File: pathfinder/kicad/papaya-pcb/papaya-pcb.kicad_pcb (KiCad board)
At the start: 2 copper layers, 70 x 90 mm, 12 parts, among them J1 J1, J10 J_S2, J11 J_S3, J12 J_S4, J2 J_ESP32, J3 J_UBEC5V, J4 J_BTS1, J5 J_BTS2, J6 J_ELRS, J7 J_GND_MASTER, J8 J_UBEC6V, J9 J_S1

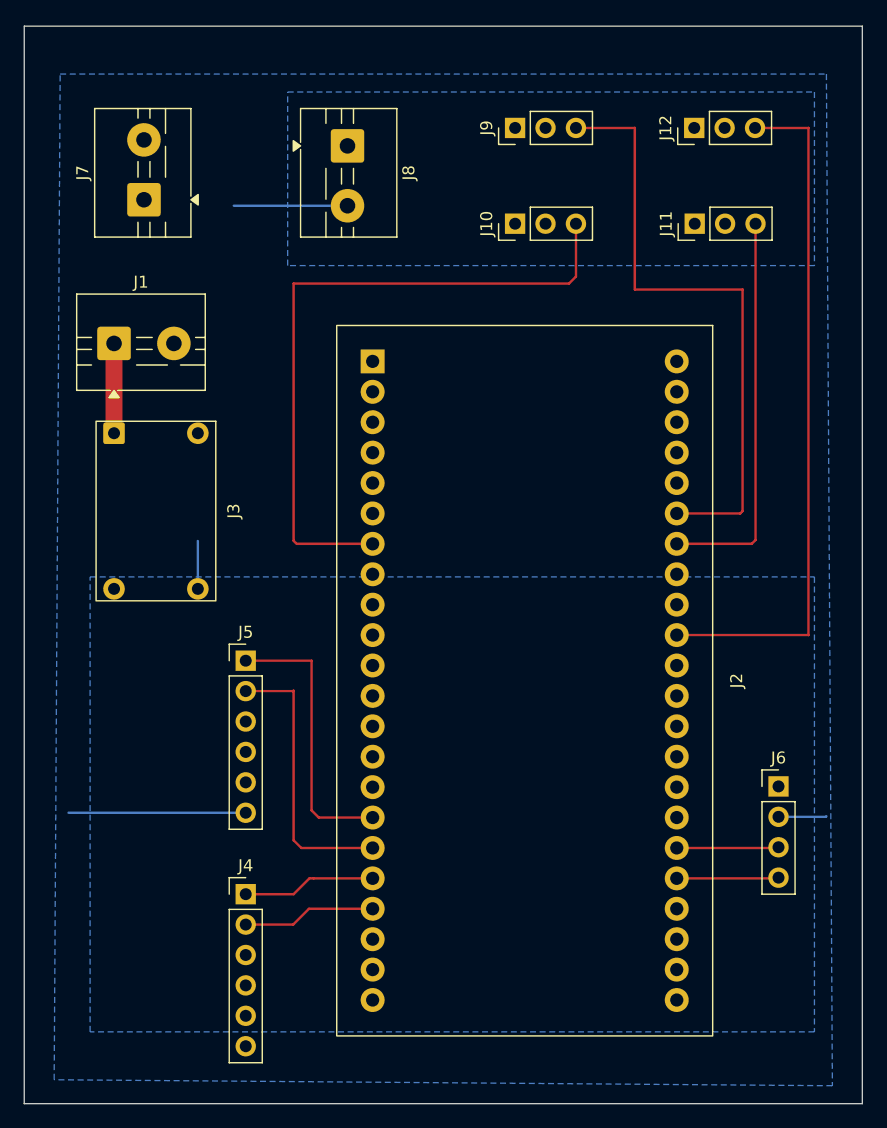
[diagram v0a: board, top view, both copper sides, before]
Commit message: Add M3 mounting holes at PCB corners
Four 3.2mm (M3 clearance) NPTH mounting holes (H1-H4) placed at the
board corners for chassis mounting. J7 and the servo header cluster
(J9-J12) were nudged to clear the new holes; zones refilled and
re-verified via DRC (0 violations).
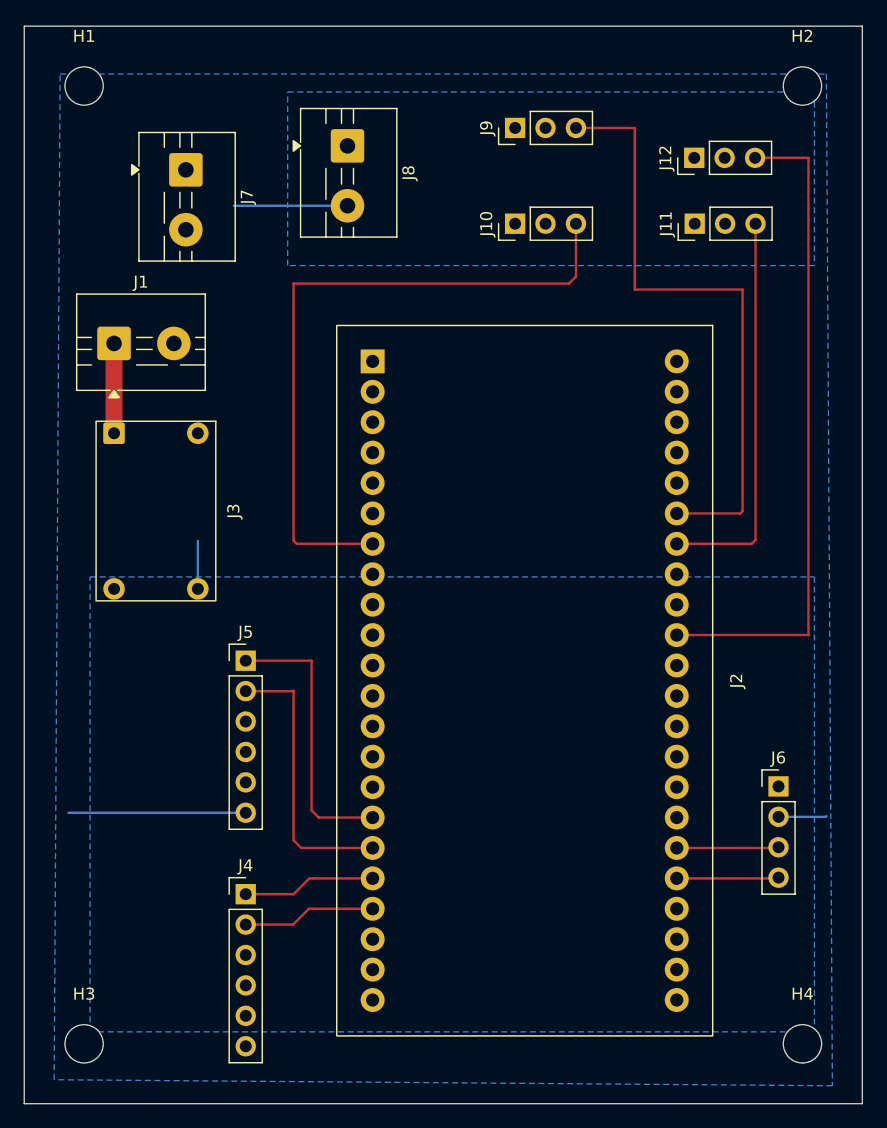
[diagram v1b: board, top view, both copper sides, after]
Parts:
- added H1: MountingHole_3.2mm_M3, MountingHole:MountingHole_3.2mm_M3, F.Cu at (95.5, 63.5)
- added H2: MountingHole_3.2mm_M3, MountingHole:MountingHole_3.2mm_M3, F.Cu at (155.5, 63.5)
- added H3: MountingHole_3.2mm_M3, MountingHole:MountingHole_3.2mm_M3, F.Cu at (95.5, 143.5)
- added H4: MountingHole_3.2mm_M3, MountingHole:MountingHole_3.2mm_M3, F.Cu at (155.5, 143.5)
- moved J7 4.30 mm to (104.0, 70.5), turned to -90 degrees
- moved J12 2.50 mm to (146.5, 69.5)
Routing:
- net /NET_S4_SIG: track 57.8 -> 55.3 mm

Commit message: Apply permanent servo-ground fix to PCB, regenerate Gerbers; v2.0.1
Cuts four zone cutouts into the 6V_POUR zone on B.Cu, one behind each
servo header GND pad (J9-J12), so MASTER_GND's lower fill priority
connects through on refill -- resolves ADR 0002 without a layer jump or
routing around signal traces. Re-verified via kicad-cli DRC (0
violations, unconnected items 5 -> 1, the remainder being a pre-existing
unrelated island) and the same point-probe technique that originally
found the defect (real ground copper now within 0.9mm of all four pads;
6V supply to each PWR pin confirmed undisturbed).

Also includes minor F.Silkscreen identification text. Gerbers/drill
files regenerated to match. No hand-wired ground jumpers needed on
boards fabricated from this revision.

Also ignores KiCad's transient *.lck session lock files.
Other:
- board text added: "BTS1"
- board text added: "BTS2"
- board text added: "ELRS"
- board text added: "S1"
- board text added: "S2"
- board text added: "S3"
- board text added: "S4"
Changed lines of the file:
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@@
 		(layer "Edge.Cuts")
+	)
+	(gr_text "S1"
+		(at 132.5 70.5 0)
+		(layer "F.SilkS")
+		(effects
+			(font
+				(size 1 1)
+				(thickness 0.1)
+			)
+			(justify left bottom)
+		)
+	)
+	(gr_text "S2"
+		(at 132.5 78.5 0)
+		(layer "F.SilkS")
+		(effects
+			(font
+				(size 1 1)
+				(thickness 0.1)
+			)
+			(justify left bottom)
+		)
+	)
+	(gr_text "S4"
+		(at 147.5 66.5 0)
+		(layer "F.SilkS")
+		(effects
+			(font
+				(size 1 1)
+				(thickness 0.1)
+			)
+			(justify left bottom)
+		)
+	)
+	(gr_text "S3"
+		(at 148 78.5 0)
+		(layer "F.SilkS")
+		(effects
+			(font
+				(size 1 1)
+				(thickness 0.1)
+			)
+			(justify left bottom)
+		)
+	)
+	(gr_text "BTS2"
+		(at 105 119 90)
+		(layer "F.SilkS")
+		(effects
+			(font
+				(size 1 1)
+				(thickness 0.1)
+			)
+			(justify left bottom)
+		)
+	)
+	(gr_text "BTS1"
+		(at 105 137 90)
+		(layer "F.SilkS")
+		(effects
+			(font
+				(size 1 1)
+				(thickness 0.1)
+			)
+			(justify left bottom)
+		)
+	)
+	(gr_text "ELRS"
+		(at 151.5 118.5 0)
+		(layer "F.SilkS")
+		(effects
+			(font
+				(size 1 1)
+				(thickness 0.15)
+				(bold yes)
+			)
+			(justify left bottom)
+		)
 	)
 	(segment
@@
 		(polygon
 			(pts
-				(xy 112.5 64) (xy 156.5 64) (xy 156.5 78.5) (xy 112.5 78.5)
-			)
-		)
+				(xy 131 67.5) (xy 132 67.5) (xy 132 64) (xy 146 64) (xy 146 70) (xy 147 70) (xy 147 64) (xy 156.5 64)
+				(xy 156.5 78.5) (xy 147 78.5) (xy 147 74.5) (xy 146 74.5) (xy 146 78.5) (xy 132 78.5) (xy 132 74.5)
+				(xy 131 74.5) (xy 131 78.5) (xy 112.5 78.5) (xy 112.5 64) (xy 131 64)
+			)
+		)
